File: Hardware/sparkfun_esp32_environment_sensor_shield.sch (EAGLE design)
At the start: 52 parts, among them J1 WEATHER_METER-WIND, J2 WEATHER_METER-RAIN, U1 BME280, U2 CCS811, U3 TSL2561FN

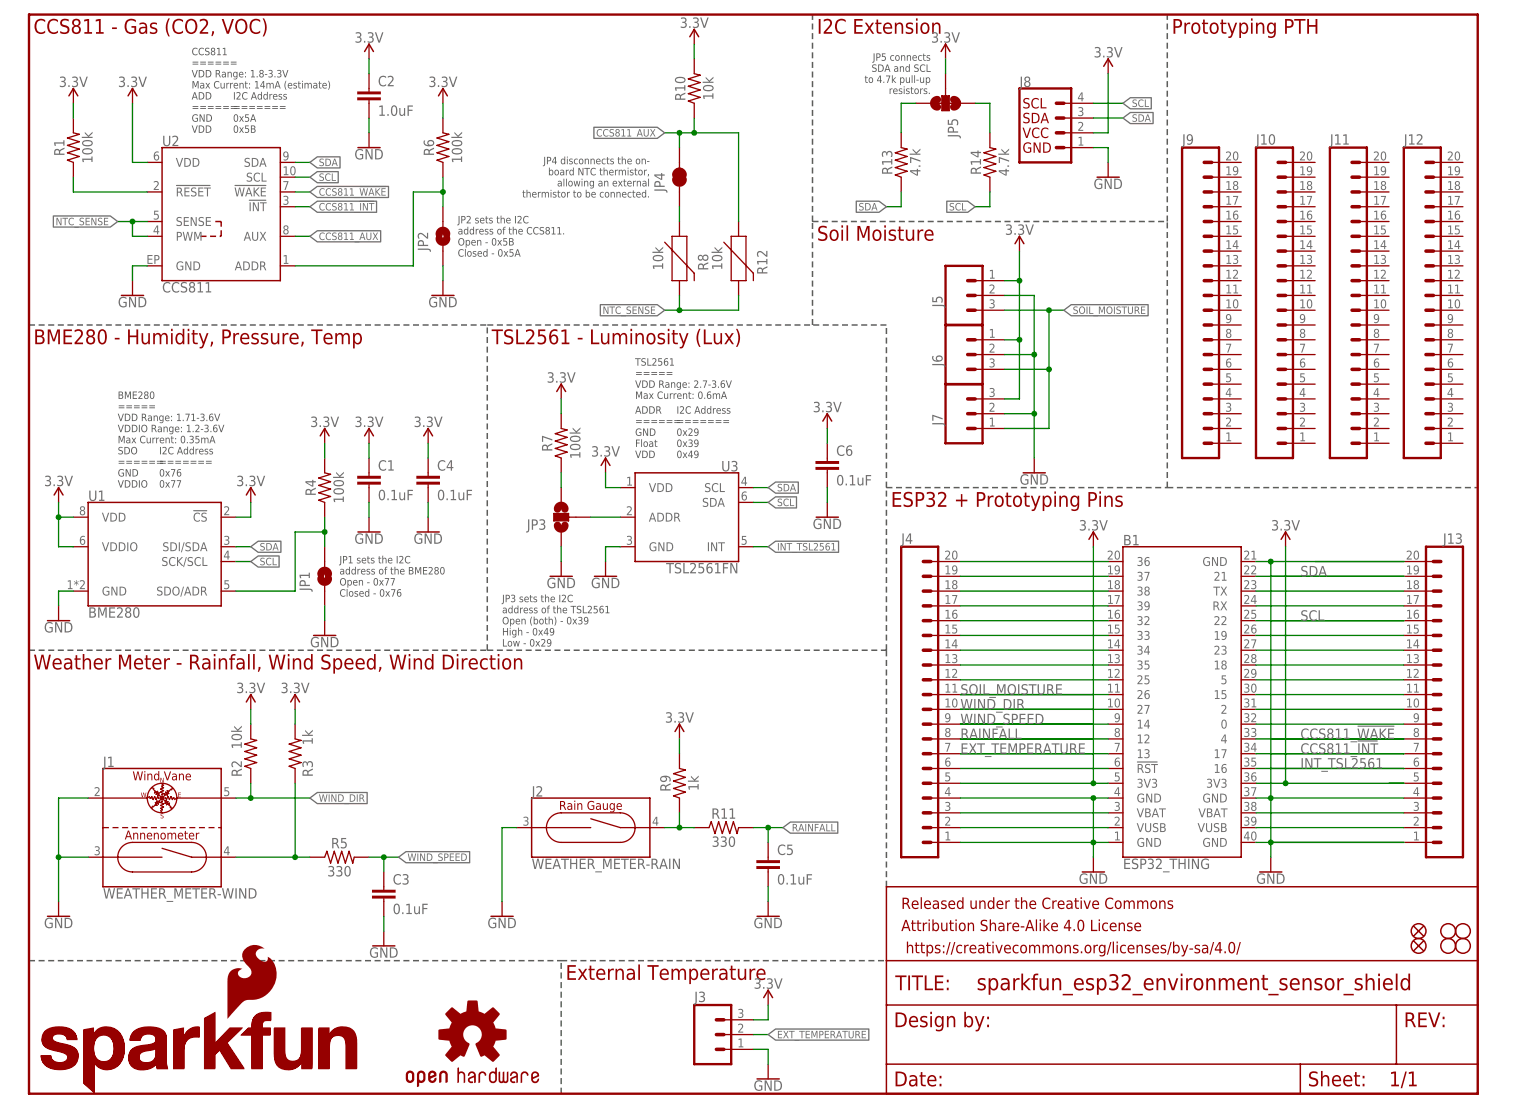
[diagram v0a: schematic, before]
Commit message: Schematic cleanup. Bussing inner prototyping pins together.
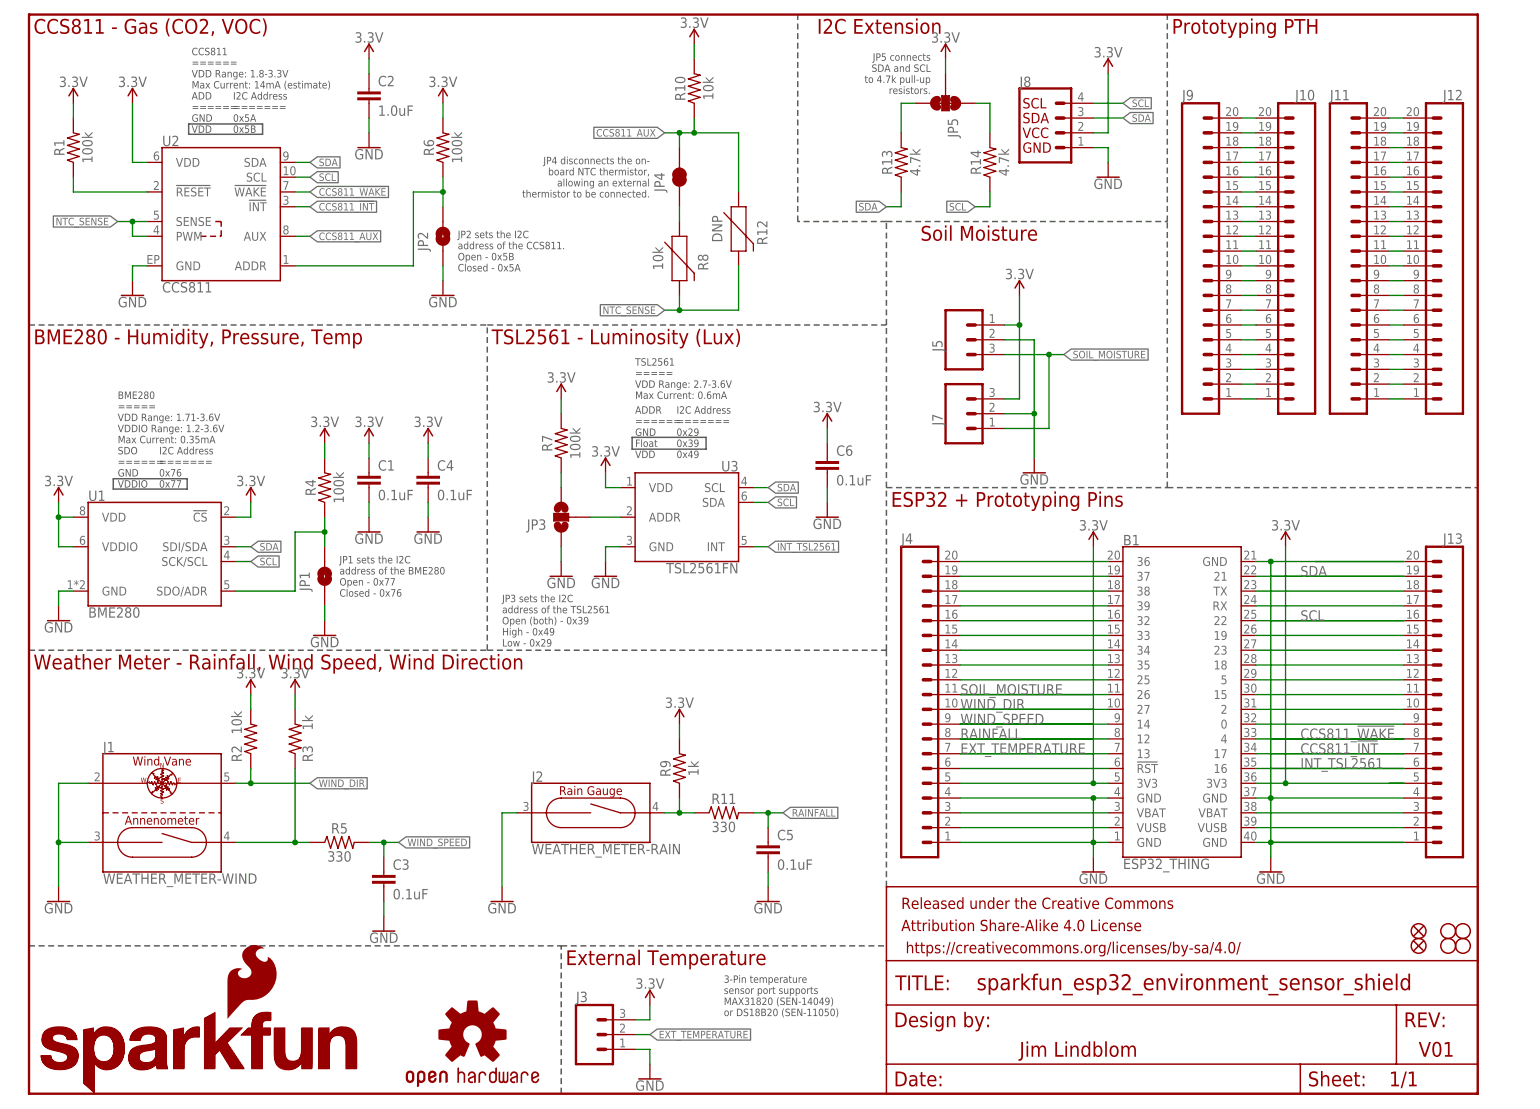
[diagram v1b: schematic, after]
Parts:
- removed J6: (no value), SparkFun-Connectors:CONN_03JST-PTH-NS
- J5: device SparkFun-Connectors:CONN_031X03_NO_SILK -> SparkFun-Connectors:CONN_03
- R12: value 10k -> DNP
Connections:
- new net N$29: J11.1, J12.1
- new net N$30: J11.2, J12.2
- new net N$31: J11.3, J12.3
- new net N$32: J11.4, J12.4
- new net N$33: J11.5, J12.5
- new net N$34: J11.6, J12.6
- new net N$35: J11.7, J12.7
- new net N$36: J11.8, J12.8
- new net N$37: J11.9, J12.9
- new net N$38: J11.10, J12.10
- new net N$39: J11.11, J12.11
- new net N$40: J11.12, J12.12
- new net N$41: J11.13, J12.13
- new net N$42: J11.14, J12.14
- new net N$43: J11.15, J12.15
- new net N$44: J11.16, J12.16
- new net N$45: J11.17, J12.17
- new net N$46: J11.18, J12.18
- new net N$47: J11.19, J12.19
- new net N$48: J11.20, J12.20
- new net N$49: J10.1, J9.1
- new net N$50: J10.2, J9.2
- new net N$51: J10.3, J9.3
- new net N$52: J10.4, J9.4
- new net N$53: J10.5, J9.5
- new net N$54: J10.6, J9.6
- new net N$55: J10.7, J9.7
- new net N$56: J10.8, J9.8
- new net N$57: J10.9, J9.9
- new net N$58: J10.10, J9.10
- new net N$59: J10.11, J9.11
- new net N$60: J10.12, J9.12
- new net N$61: J10.13, J9.13
- new net N$62: J10.14, J9.14
- new net N$63: J10.15, J9.15
- new net N$64: J10.16, J9.16
- new net N$65: J10.17, J9.17
- new net N$66: J10.18, J9.18
- new net N$67: J10.19, J9.19
- new net N$68: J10.20, J9.20
- net 3.3V: no longer J6.1
- net GND: no longer J6.2
- net SOIL_MOISTURE: no longer J6.3
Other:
- note added: "3-Pin temperature sensor port supports MAX31820 (SEN-14049) or DS18B20 (SEN-11050)"
- note added: "Jim Lindblom"
- note added: "V01"
- moved on the sheet: C3, C5, J1, J10, J11, J12, J2, J3, J5, J9, R11, R12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

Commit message: Connecting CCS811 RST pin to ESP32.
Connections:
- removed net N$22: B1.15, J13.11
- net CCS811_!RST!: now also B1.4, J13.8
- net CCS811_!WAKE!: now also B1.15, J13.11; no longer B1.4, J13.8
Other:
- moved on the sheet: C2, JP2, R1, R6, U2

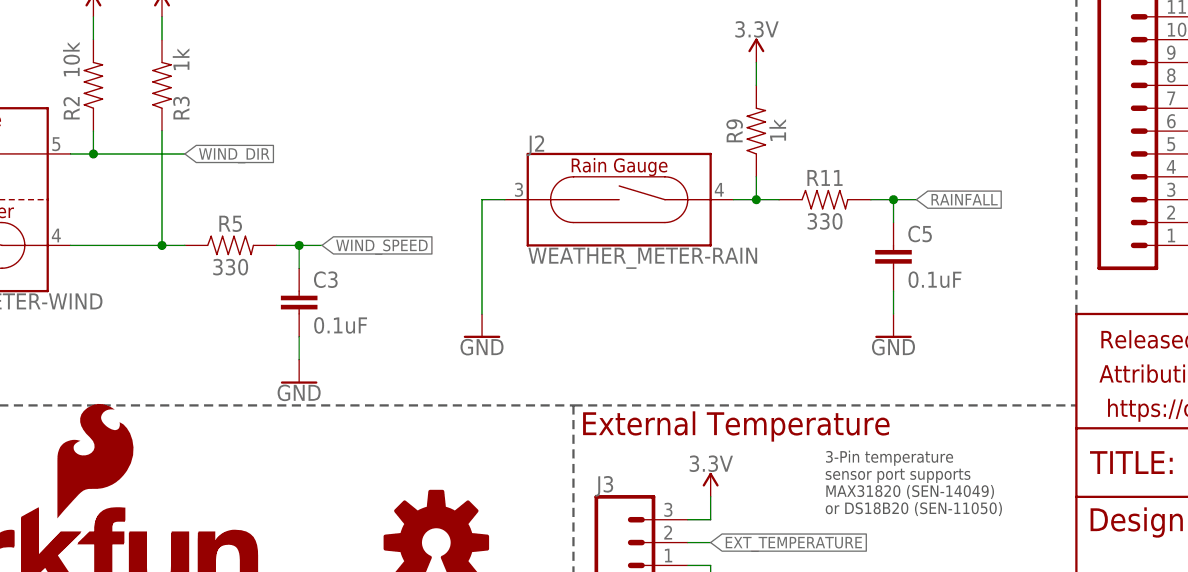
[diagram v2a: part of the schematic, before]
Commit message: Revising weather meter circuits after tests with ESP32 Thing.
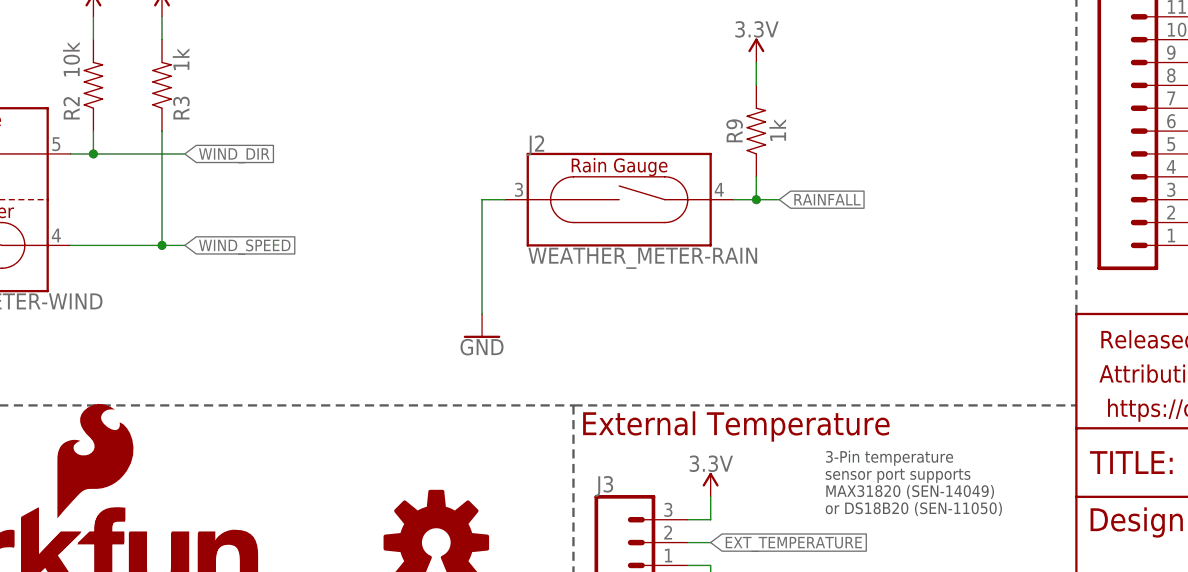
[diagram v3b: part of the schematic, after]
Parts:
- removed C3, C5: 0.1uF, SparkFun-Capacitors:0.1UF-0603-25V-(+80/-20%)
- removed R11, R5: 330, SparkFun-Resistors:330OHM-0603-1/10W-1%
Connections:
- removed net RAIN_OUT: J2.2, R11.1, R9.1
- removed net WIND_OUT: J1.ANN-2, R3.1, R5.1
- net GND: no longer C3.2, C5.2
- net RAINFALL: now also J2.2, R9.1; no longer C5.1, R11.2
- net WIND_SPEED: now also J1.ANN-2, R3.1; no longer C3.1, R5.2
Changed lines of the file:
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@@
 <part name="R3" library="SparkFun-Resistors" deviceset="1KOHM" device="-0603-1/10W-1%" value="1k"/>
 <part name="SUPPLY14" library="SparkFun-PowerSymbols" deviceset="3.3V" device=""/>
-<part name="R11" library="SparkFun-Resistors" deviceset="330OHM" device="-0603-1/10W-1%" value="330"/>
-<part name="C5" library="SparkFun-Capacitors" deviceset="0.1UF" device="-0603-25V-(+80/-20%)" value="0.1uF"/>
-<part name="GND13" library="SparkFun-PowerSymbols" deviceset="GND" device=""/>
-<part name="R5" library="SparkFun-Resistors" deviceset="330OHM" device="-0603-1/10W-1%" value="330"/>
-<part name="C3" library="SparkFun-Capacitors" deviceset="0.1UF" device="-0603-25V-(+80/-20%)" value="0.1uF"/>
-<part name="GND7" library="SparkFun-PowerSymbols" deviceset="GND" device=""/>
 <part name="SUPPLY6" library="SparkFun-PowerSymbols" deviceset="3.3V" device=""/>
 <part name="J3" library="SparkFun-Connectors" deviceset="CONN_03" device=""/>
@@
 </instance>
 <instance part="SUPPLY14" gate="G$1" x="111.76" y="63.5"/>
-<instance part="R11" gate="G$1" x="119.38" y="48.26"/>
-<instance part="C5" gate="G$1" x="127" y="40.64"/>
-<instance part="GND13" gate="1" x="127" y="33.02" rot="MR0"/>
-<instance part="R5" gate="G$1" x="53.34" y="43.18"/>
-<instance part="C3" gate="G$1" x="60.96" y="35.56"/>
-<instance part="GND7" gate="1" x="60.96" y="27.94"/>
 <instance part="SUPPLY6" gate="G$1" x="45.72" y="68.58"/>
 <instance part="J3" gate="J$1" x="96.52" y="10.16"/>
@@
 </segment>
 <segment>
-<pinref part="C5" gate="G$1" pin="2"/>
-<pinref part="GND13" gate="1" pin="GND"/>
-<wire x1="127" y1="35.56" x2="127" y2="38.1" width="0.1524" layer="91"/>
-</segment>
-<segment>
-<pinref part="C3" gate="G$1" pin="2"/>
-<pinref part="GND7" gate="1" pin="GND"/>
-<wire x1="60.96" y1="30.48" x2="60.96" y2="33.02" width="0.1524" layer="91"/>
-</segment>
-<segment>
 <pinref part="J3" gate="J$1" pin="1"/>
 <wire x1="104.14" y1="7.62" x2="106.68" y2="7.62" width="0.1524" layer="91"/>
@@
 <net name="RAINFALL" class="0">
 <segment>
-<pinref part="R11" gate="G$1" pin="2"/>
-<pinref part="C5" gate="G$1" pin="1"/>
-<wire x1="124.46" y1="48.26" x2="127" y2="48.26" width="0.1524" layer="91"/>
-<wire x1="127" y1="48.26" x2="127" y2="45.72" width="0.1524" layer="91"/>
-<wire x1="127" y1="48.26" x2="129.54" y2="48.26" width="0.1524" layer="91"/>
-<junction x="127" y="48.26"/>
-<label x="129.54" y="48.26" size="1.27" layer="95" xref="yes"/>
+<label x="114.3" y="48.26" size="1.27" layer="95" xref="yes"/>
+<pinref part="J2" gate="G$1" pin="2"/>
+<wire x1="109.22" y1="48.26" x2="111.76" y2="48.26" width="0.1524" layer="91"/>
+<pinref part="R9" gate="G$1" pin="1"/>
+<wire x1="111.76" y1="48.26" x2="111.76" y2="50.8" width="0.1524" layer="91"/>
+<wire x1="114.3" y1="48.26" x2="111.76" y2="48.26" width="0.1524" layer="91"/>
+<junction x="111.76" y="48.26"/>
 </segment>
 <segment>
@@
 <net name="WIND_SPEED" class="0">
 <segment>
-<pinref part="R5" gate="G$1" pin="2"/>
-<pinref part="C3" gate="G$1" pin="1"/>
-<wire x1="58.42" y1="43.18" x2="60.96" y2="43.18" width="0.1524" layer="91"/>
-<wire x1="60.96" y1="43.18" x2="60.96" y2="40.64" width="0.1524" layer="91"/>
-<wire x1="60.96" y1="43.18" x2="63.5" y2="43.18" width="0.1524" layer="91"/>
-<junction x="60.96" y="43.18"/>
-<label x="63.5" y="43.18" size="1.27" layer="95" xref="yes"/>
+<label x="48.26" y="43.18" size="1.27" layer="95" xref="yes"/>
+<pinref part="J1" gate="G$1" pin="ANN-2"/>
+<wire x1="35.56" y1="43.18" x2="45.72" y2="43.18" width="0.1524" layer="91"/>
+<pinref part="R3" gate="G$1" pin="1"/>
+<wire x1="45.72" y1="55.88" x2="45.72" y2="43.18" width="0.1524" layer="91"/>
+<junction x="45.72" y="43.18"/>
+<wire x1="48.26" y1="43.18" x2="45.72" y2="43.18" width="0.1524" layer="91"/>
 </segment>
 <segment>
@@
 </segment>
 </net>
-<net name="RAIN_OUT" class="0">
-<segment>
-<pinref part="J2" gate="G$1" pin="2"/>
-<wire x1="109.22" y1="48.26" x2="111.76" y2="48.26" width="0.1524" layer="91"/>
-<pinref part="R9" gate="G$1" pin="1"/>
-<wire x1="111.76" y1="48.26" x2="111.76" y2="50.8" width="0.1524" layer="91"/>
-<wire x1="111.76" y1="48.26" x2="114.3" y2="48.26" width="0.1524" layer="91"/>
-<junction x="111.76" y="48.26"/>
-<pinref part="R11" gate="G$1" pin="1"/>
-</segment>
-</net>
-<net name="WIND_OUT" class="0">
-<segment>
-<pinref part="J1" gate="G$1" pin="ANN-2"/>
-<pinref part="R5" gate="G$1" pin="1"/>
-<wire x1="35.56" y1="43.18" x2="45.72" y2="43.18" width="0.1524" layer="91"/>
-<pinref part="R3" gate="G$1" pin="1"/>
-<wire x1="45.72" y1="43.18" x2="48.26" y2="43.18" width="0.1524" layer="91"/>
-<wire x1="45.72" y1="55.88" x2="45.72" y2="43.18" width="0.1524" layer="91"/>
-<junction x="45.72" y="43.18"/>
-</segment>
-</net>

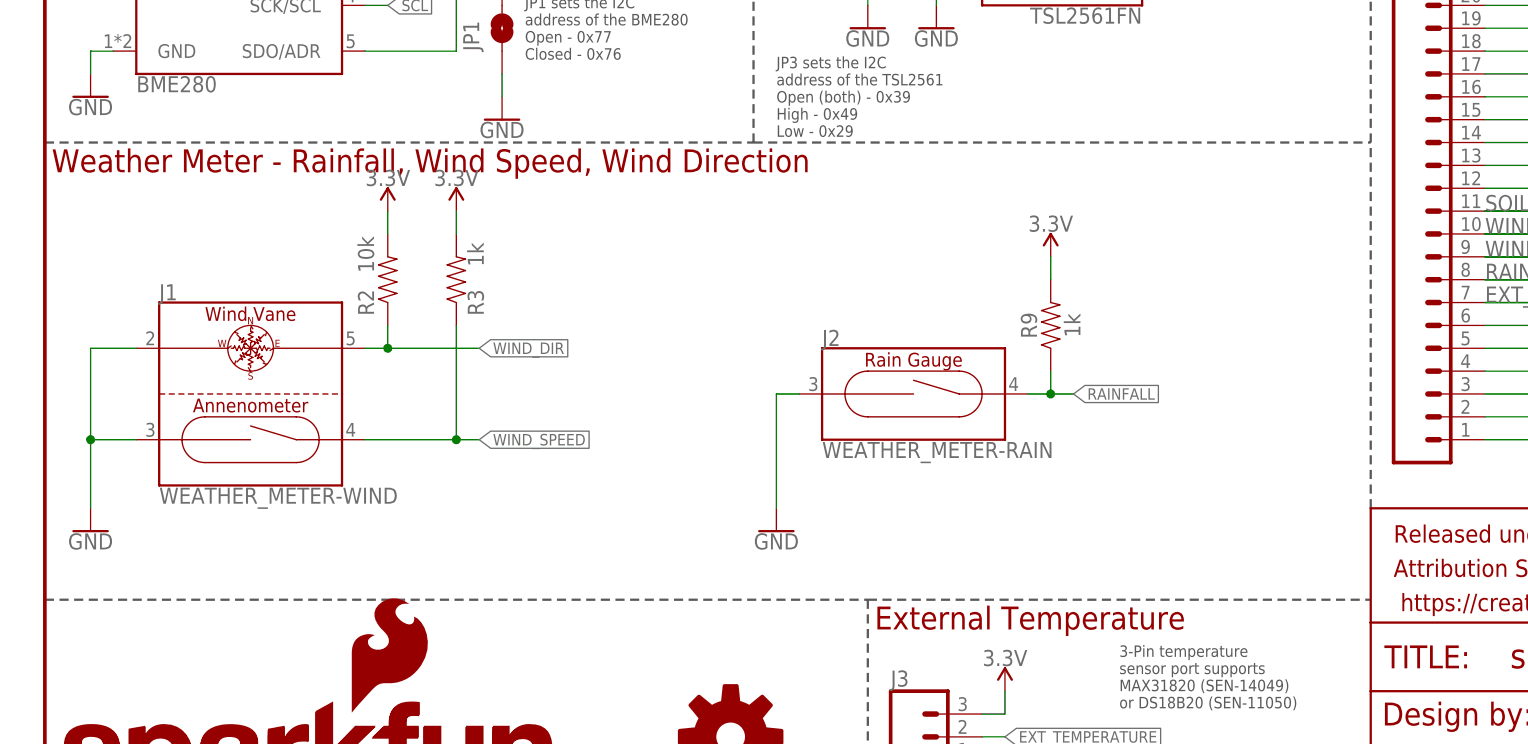
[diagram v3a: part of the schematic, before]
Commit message: Adding TVS diode to weather meter signals.
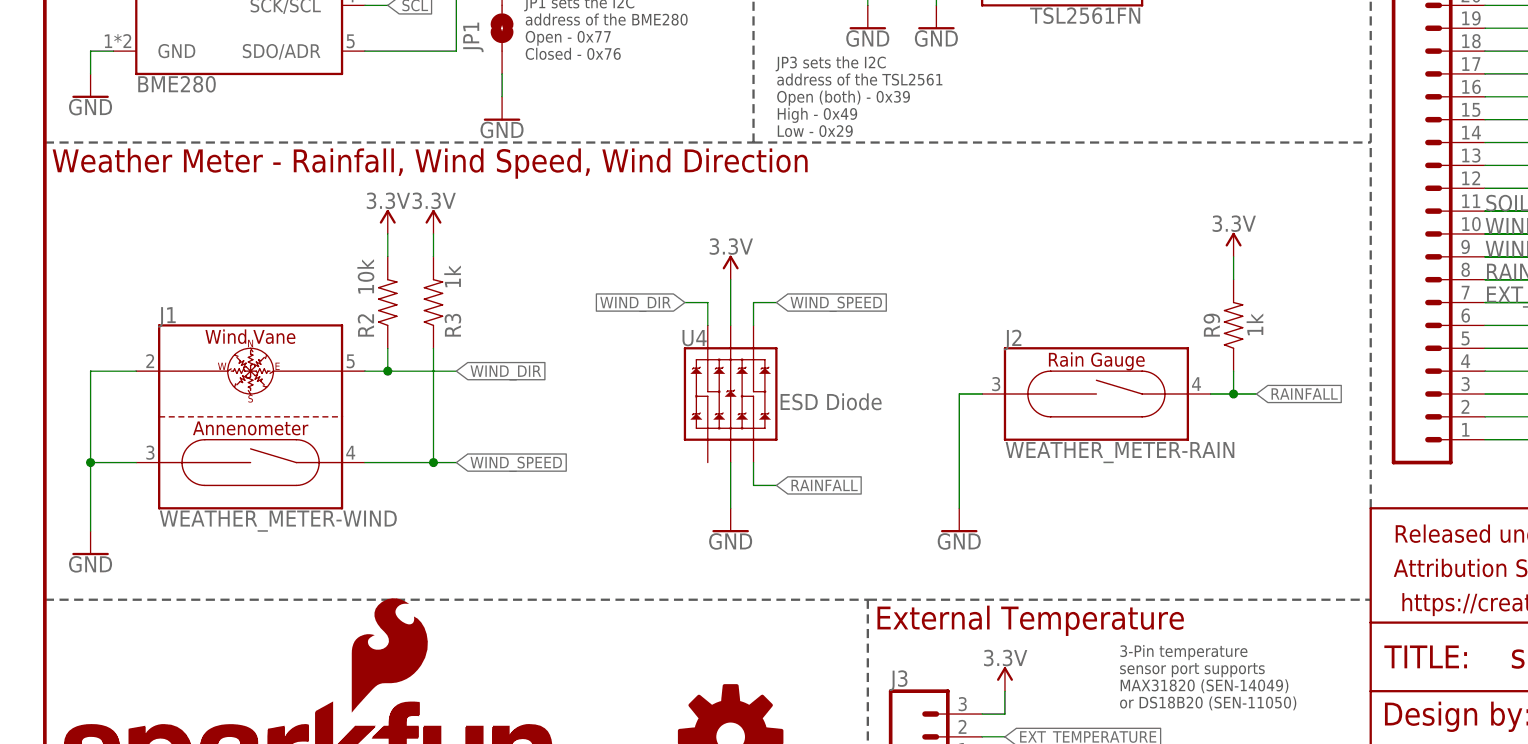
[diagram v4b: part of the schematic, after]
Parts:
- added U4: ESD Diode, esp32-environ-monitor-temp:TVS_DIODE_ARRAYSMD
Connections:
- net 3.3V: now also U4.VCC
- net GND: now also U4.VSS
- net RAINFALL: now also U4.IO2
- net WIND_DIR: now also U4.IO4
- net WIND_SPEED: now also U4.IO3
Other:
- moved on the sheet: J1, J2, R2, R3, R9
